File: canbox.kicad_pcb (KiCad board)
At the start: 2 copper layers, 99 x 70 mm, 125 parts, among them J1 SWD, J11 USB_B_Micro, J2 RELAY, J3 100BaseT1, J4 USB_B_Micro, J5 DB9_Male, J6 Conn_01x08_Female, J7 USB_B_Micro, J9 USB_B_Micro, K2 FTR-K3AB005W, U1 LPC54616J512, U11 MP1582EN-LF-Z, U2 DP83TC811R-Q1, U3 74LVC1G04, U5 TJA1051T/3/1J, U6 TLV70233_SOT23-5, U7 KeyMatrix, U8 ULN2003ADRG3, Y1 12MHZ, Y2 25 MHz

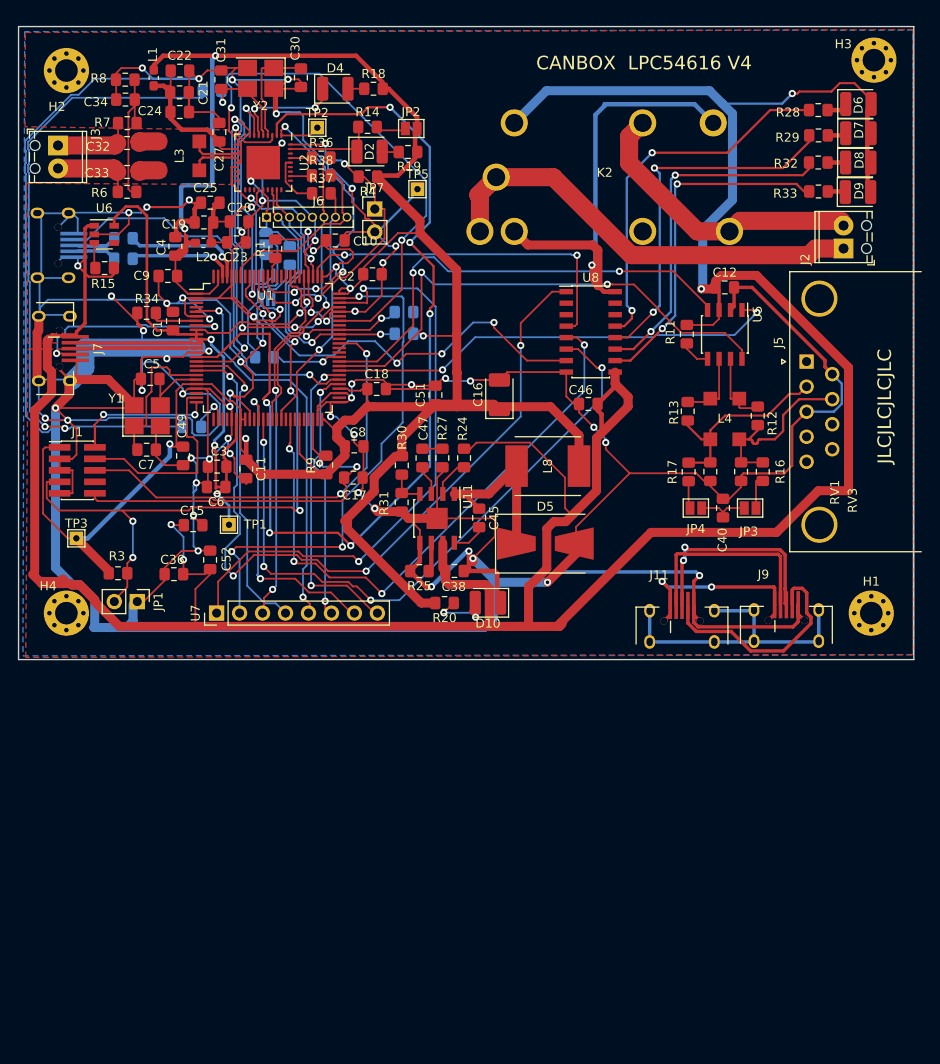
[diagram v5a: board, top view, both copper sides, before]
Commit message: Switch to 4 Layer PCB as the RMII loopback doesn't work
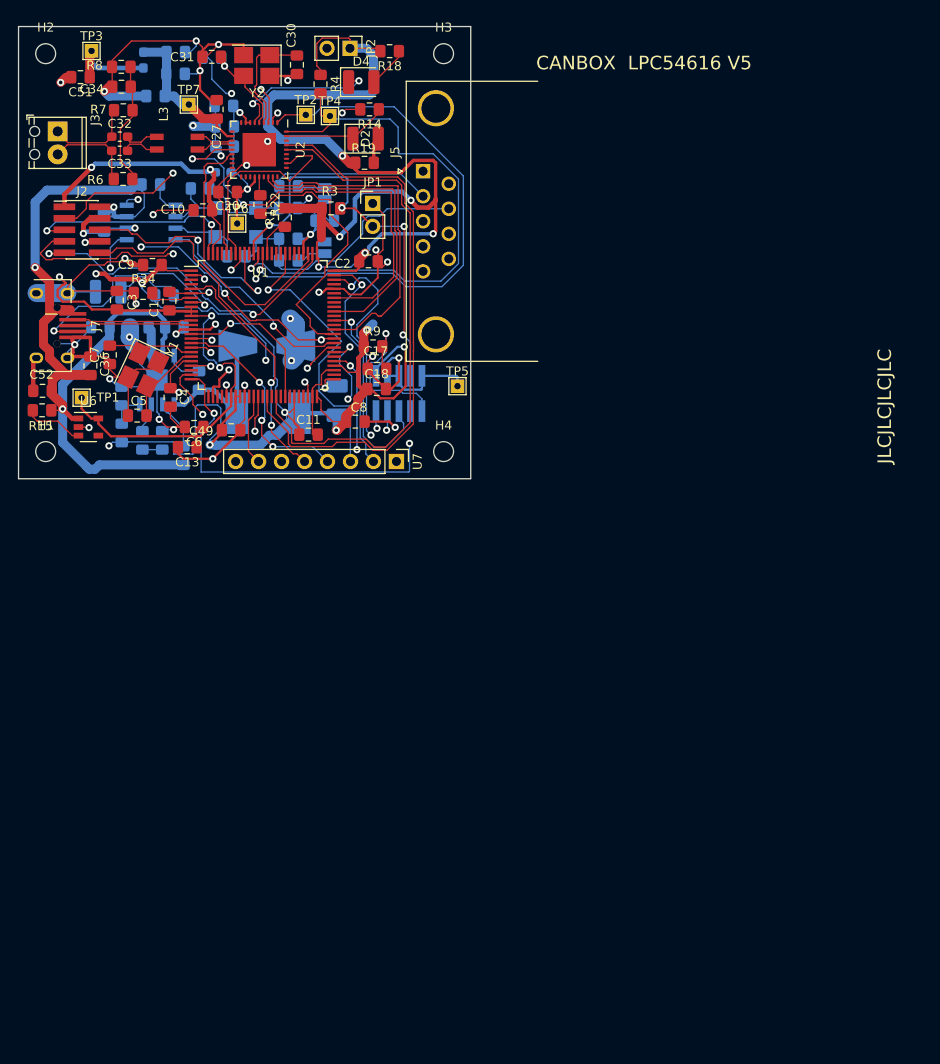
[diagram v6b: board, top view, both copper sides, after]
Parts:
- removed C15: 100n, Capacitor_SMD:C_0805_2012Metric_Pad1.15x1.40mm_HandSolder
- removed D6, D7, D8, D9: LED, LED_SMD:LED_1210_3225Metric
- removed J11, J4, J9: USB_B_Micro, cypress:MicroUsb
- removed J6: Conn_01x08_Female, Connector_PinHeader_1.27mm:PinHeader_1x08_P1.27mm_Vertical_RMII
- removed JP5: Jumper_3_Bridged12, Jumper:SolderJumper-3_P1.3mm_Open_RoundedPad1.0x1.5mm
- removed JP7: MDIO, Connector_PinHeader_2.54mm:PinHeader_1x02_P2.54mm_Vertical
- removed K2: FTR-K3AB005W, cypress:ALF1T05
- removed R10, R5: 2.49k, Resistor_SMD:R_0805_2012Metric_Pad1.15x1.40mm_HandSolder
- removed R2, R21, R23: 33, Resistor_SMD:R_0805_2012Metric_Pad1.15x1.40mm_HandSolder
- removed R28, R29, R32, R33: 300, Resistor_SMD:R_0805_2012Metric_Pad1.15x1.40mm_HandSolder
- removed R35, R36, R37, R38: NM, Resistor_SMD:R_0805_2012Metric_Pad1.15x1.40mm_HandSolder
- removed U3: 74LVC1G04, Package_TO_SOT_SMD:SOT-353_SC-70-5_Handsoldering
- removed U8: ULN2003ADRG3, Package_SO:SOIC-16_3.9x9.9mm_P1.27mm
- added C13: 4.7u, Capacitor_SMD:C_0805_2012Metric_Pad1.15x1.40mm_HandSolder, F.Cu at (38.7, 66.5)
- added TP4: MDIO, TestPoint:TestPoint_THTPad_1.5x1.5mm_Drill0.7mm, F.Cu at (54.4, 29.9)
- added TP6: ETH_IO, TestPoint:TestPoint_THTPad_1.5x1.5mm_Drill0.7mm, F.Cu at (44.2, 41.8)
- added TP7: ETH_A, TestPoint:TestPoint_THTPad_1.5x1.5mm_Drill0.7mm, F.Cu at (38.8, 28.6)
- C12, C16, C19, C21, C22, C23, C24, C25, C38, C40, C45, C46, C47, D10, D5, J1, JP3, JP4, L1, L2, L4, L8, R11, R12, R13, R16, R17, R20, R24, R25, R27, RV1, RV3, U11, U5: moved to B.Cu
- C32, C33: footprint Capacitor_SMD:C_0805_2012Metric_Pad1.15x1.40mm_HandSolder -> Capacitor_SMD:C_0603_1608Metric_Pad1.05x0.95mm_HandSolder
- C6: value 4.7u -> 10n
- H1, H2, H3, H4: value H -> MountingHole-Mechanical; footprint MountingHole:MountingHole_2.5mm_Pad_Via -> MountingHole:MountingHole_2.2mm_M2_DIN965
- J2: value RELAY -> Conn_02x05_Odd_Even; footprint TerminalBlock_Phoenix:TerminalBlock_Phoenix_MPT-0,5-2-2.54_1x02_P2.54mm_Horizontal -> Connector_PinHeader_1.27mm:PinHeader_2x05_P1.27mm_Vertical_SMD
- JP2: footprint Jumper:SolderJumper-2_P1.3mm_Open_Pad1.0x1.5mm -> Connector_PinHeader_2.54mm:PinHeader_1x02_P2.54mm_Vertical
- R22: moved to F.Cu
- R30: value 124k -> 12.4k; moved to B.Cu
- R31: value 39.2k -> 3.9k; moved to B.Cu
- moved H1 93.0 mm to (23.0, 67.0)
- moved J2 84.2 mm to (27.0, 42.5), turned to 0 degrees
- moved C12 69.0 mm to (29.5, 41.7), turned to 270 degrees
- moved U5 64.6 mm to (34.7, 41.7), turned to 0 degrees
- moved R11 61.5 mm to (34.6, 37.5), turned to 0 degrees
- moved R12 60.3 mm to (44.1, 45.4), turned to 0 degrees
- moved R13 59.3 mm to (40.1, 37.9), turned to 0 degrees
- moved L4 58.3 mm to (44.0, 41.7), turned to 180 degrees
- moved R16 57.4 mm to (49.8, 45.9), turned to 0 degrees
- moved RV3 56.3 mm to (49.8, 43.5), turned to 0 degrees
- moved JP3 55.1 mm to (53.9, 44.5), turned to 270 degrees
- moved RV1 55.0 mm to (49.8, 40.1), turned to 0 degrees
- moved C46 54.6 mm to (29.0, 53.2)
- moved R17 54.4 mm to (49.9, 37.7), turned to 0 degrees
- moved C40 54.3 mm to (53.9, 41.5), turned to 180 degrees
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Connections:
- J1 pad 8: Net-(J1-Pad8) -> (no net)
- J2 pad 1: Net-(J2-Pad1) -> +3V3
- J2 pad 2: Net-(J2-Pad2) -> +5V
- J5 pad 1: Net-(J5-Pad1) -> (no net)
- J5 pad 4: Net-(J5-Pad4) -> (no net)
- J5 pad 5: Net-(J5-Pad5) -> (no net)
- J5 pad 8: Net-(J5-Pad8) -> (no net)
- J5 pad 9: Net-(J5-Pad9) -> (no net)
- R22 pad 1: Net-(JP5-Pad2) -> /Ethernet/RGMII_CLK
- U1 pad 100: Net-(U1-Pad100) -> Net-(J2-Pad5)
- U1 pad 18: Net-(U1-Pad18) -> Net-(J2-Pad3)
- U1 pad 27: Net-(R35-Pad2) -> Net-(R26-Pad2)
- U1 pad 28: Net-(U1-Pad28) -> (no net)
- U1 pad 29: Net-(U1-Pad29) -> (no net)
- U1 pad 3: Net-(U1-Pad3) -> (no net)
- U1 pad 37: Net-(U1-Pad37) -> Net-(J2-Pad8)
- U1 pad 4: Net-(U1-Pad4) -> (no net)
- U1 pad 43: Net-(U1-Pad43) -> Net-(J2-Pad10)
- U1 pad 44: Net-(U1-Pad44) -> (no net)
- U1 pad 47: Net-(U1-Pad47) -> (no net)
- U1 pad 52: Net-(U1-Pad52) -> (no net)
- U1 pad 56: Net-(J4-Pad4) -> (no net)
- U1 pad 62: (no net) -> /Ethernet/RGMII_DO
- U1 pad 65: Net-(U1-Pad65) -> (no net)
- U1 pad 67: /Ethernet/RGMII_DO -> (no net)
- U1 pad 70: Net-(U1-Pad70) -> (no net)
- U1 pad 72: Net-(U1-Pad72) -> (no net)
- U1 pad 77: Net-(U1-Pad77) -> Net-(J2-Pad9)
- U1 pad 80: /3V3_LC -> (no net)
- U1 pad 82: Net-(U1-Pad82) -> (no net)
- U1 pad 85: Net-(U1-Pad85) -> (no net)
- U1 pad 91: Net-(U1-Pad91) -> (no net)
- U1 pad 92: Net-(U1-Pad92) -> Net-(J2-Pad6)
- U1 pad 93: Net-(U1-Pad93) -> Net-(J2-Pad7)
- U1 pad 95: Net-(U1-Pad95) -> (no net)
- U1 pad 97: /PowerSupply/USB0_D+ -> (no net)
- U1 pad 98: /PowerSupply/USB0_D- -> (no net)
- U2 pad 29: Net-(R38-Pad1) -> /Ethernet/RGMII_TX_EN
- U2 pad 32: Net-(R37-Pad1) -> /Ethernet/RGMII_TX_D1
- U2 pad 33: Net-(R36-Pad1) -> /Ethernet/RGMII_TX_D0
- U2 pad 7: Net-(U1-Pad91) -> /Ethernet/ETH_3V3
- U2 pad 8: Net-(U1-Pad72) -> /Ethernet/ETH_3V3
- U6 pad 4: Net-(U6-Pad4) -> (no net)
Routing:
- net GND: track 891.5 -> 543.5 mm, vias 60 -> 41
- net +5V: track 383.8 -> 104.9 mm, vias 5 -> 3
- net +3V3: track 317.6 -> 411.3 mm, vias 9 -> 17
- net Net-(U1-Pad18): track 84.7 -> 0.00 mm, vias 4 -> 0
- net Net-(U1-Pad37): track 72.6 -> 0.00 mm, vias 4 -> 0
- net Net-(U1-Pad15): track 112.1 -> 42.7 mm, vias 6 -> 3
- net Net-(U1-Pad43): track 66.3 -> 0.00 mm, vias 4 -> 0
- net Net-(K2-Pad1): track 50.0 -> 0.00 mm, vias 1 -> 0
- net Net-(J2-Pad1): track 49.2 -> 0.00 mm
- net Net-(U1-Pad92): track 46.5 -> 0.00 mm, vias 4 -> 0
- net Net-(J4-Pad4): track 43.1 -> 0.00 mm, vias 1 -> 0
- net Net-(R28-Pad1): track 41.2 -> 0.00 mm, vias 2 -> 0
- net Net-(R29-Pad1): track 40.9 -> 0.00 mm, vias 2 -> 0
- net Net-(J2-Pad8): track 0.00 -> 40.8 mm, vias 0 -> 2
- net Net-(J2-Pad3): track 0.00 -> 40.0 mm, vias 0 -> 2
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- added copper zone on In1.Cu, net (none)
- added copper zone on In2.Cu, net GND
- removed copper zone on B.Cu, net GND
- removed copper zone on F.Cu, net GND
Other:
- board size 99 x 70 mm -> 50 x 50 mm
- copper layers 2 -> 4
- net class Default: clearance 0.127 -> 0.2; trace_width 0.24 -> 0.146812
- net class DiffPair added: clearance 0.127, trace_width 1, via_dia 0.8, via_drill 0.4
- net class DiffPairUSB added: clearance 0.127, trace_width 1, via_dia 0.8, via_drill 0.4
- rule trace_clearance: 0.127 -> 0.2
- rule trace_min: 0.1905 -> 0.1016
- rule via_min_drill: 0.3 -> 0.4
- board text added: "CANBOX LPC54616 V5"
- board text added: "JLC2313 50 Ohm 5.78 mil 100 Ohmm 4 mil 5 mil gap"
- board text removed: "CANBOX LPC54616 V4"

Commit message: V5 now impedance controlled
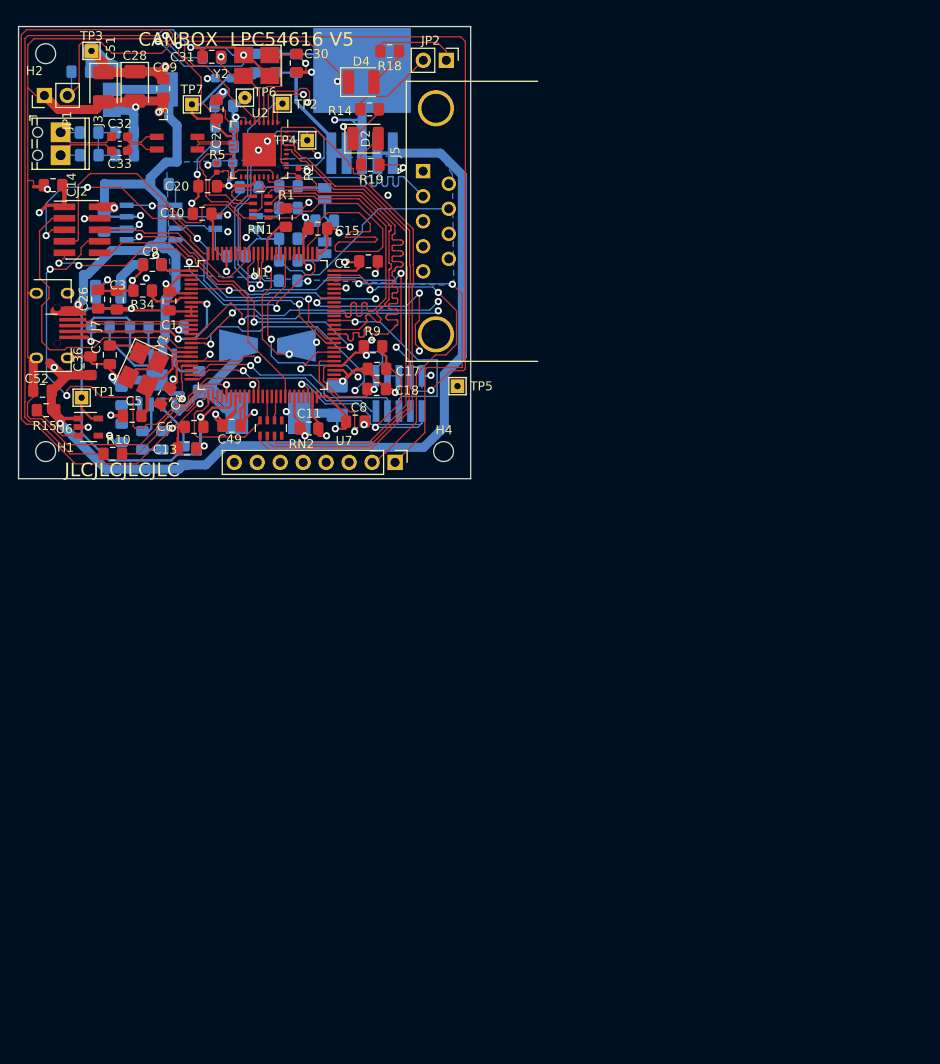
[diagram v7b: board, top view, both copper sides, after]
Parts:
- removed H3: MountingHole-Mechanical, MountingHole:MountingHole_2.2mm_M2_DIN965
- removed R22: 33, Resistor_SMD:R_0805_2012Metric_Pad1.15x1.40mm_HandSolder
- added C14: 100n, Capacitor_SMD:C_0805_2012Metric_Pad1.15x1.40mm_HandSolder, F.Cu at (23.8, 37.5)
- added C15: 100n, Capacitor_SMD:C_0805_2012Metric_Pad1.15x1.40mm_HandSolder, F.Cu at (53.1, 42.3)
- added C26: 100n, Capacitor_SMD:C_0805_2012Metric_Pad1.15x1.40mm_HandSolder, F.Cu at (28.8, 50.2)
- added C28: NM, Capacitor_Tantalum_SMD:CP_EIA-3528-21_Kemet-B_Pad1.50x2.35mm_HandSolder, F.Cu at (32.9, 26.6)
- added C29: NM, Capacitor_SMD:C_0805_2012Metric_Pad1.15x1.40mm_HandSolder, F.Cu at (36.0, 26.9)
- added R10: NM, Resistor_SMD:R_0805_2012Metric_Pad1.15x1.40mm_HandSolder, F.Cu at (30.4, 67.2)
- added R2: 2.49k, Resistor_SMD:R_0402_1005Metric, F.Cu at (50.9, 36.2)
- added R5: 2.49k, Resistor_SMD:R_0402_1005Metric, F.Cu at (41.9, 35.6)
- added RN1: 50, Resistor_SMD:R_Array_Concave_4x0603, F.Cu at (46.8, 40.0)
- added RN2: 50, Resistor_SMD:R_Array_Concave_4x0603, F.Cu at (47.9, 64.4)
- added U3: TL1963A, Package_TO_SOT_SMD:TO-263-5_TabPin3, B.Cu at (58.0, 28.2)
- added U4: AP2114H-3.3, Package_TO_SOT_SMD:SOT-223-3_TabPin2, B.Cu at (33.5, 27.0)
- C34, R3, R4, R6, R7, R8: moved to B.Cu
- C51: footprint Capacitor_SMD:C_0805_2012Metric_Pad1.15x1.40mm_HandSolder -> Capacitor_Tantalum_SMD:CP_EIA-3528-21_Kemet-B_Pad1.50x2.35mm_HandSolder
- L3, L4: footprint Inductor_SMD:L_CMC_1812 -> cypress:L_CMC_1812
- moved JP1 38.2 mm to (22.9, 27.6), turned to 90 degrees
- moved R3 31.5 mm to (26.9, 25.0), turned to 0 degrees
- moved R4 22.0 mm to (49.8, 48.1), turned to 180 degrees
- moved C24 16.0 mm to (50.7, 24.1), turned to 90 degrees
- moved TP6 13.9 mm to (45.0, 27.9)
- moved C22 11.1 mm to (48.5, 24.0), turned to 90 degrees
- moved JP2 10.7 mm to (67.3, 23.7)
- moved R8 9.79 mm to (31.7, 34.2), turned to 0 degrees
- moved L1 9.05 mm to (42.6, 25.7), turned to 0 degrees
- moved C21 8.90 mm to (46.2, 24.0), turned to 90 degrees
- moved R13 5.43 mm to (45.5, 37.8)
- moved C34 5.08 mm to (31.7, 31.7), turned to 180 degrees
- moved R6 4.56 mm to (27.8, 34.2)
- moved R7 4.52 mm to (27.8, 31.7)
- moved TP4 3.68 mm to (51.9, 32.6)
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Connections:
- R26 pad 2: Net-(R26-Pad2) -> Net-(R10-Pad1)
- U1 pad 26: (no net) -> Net-(RN2-Pad4)
- U1 pad 27: Net-(R26-Pad2) -> Net-(R10-Pad2)
- U1 pad 39: /Ethernet/RGMII_TX_D0 -> Net-(RN2-Pad3)
- U1 pad 41: /Ethernet/RGMII_TX_D1 -> Net-(RN2-Pad2)
- U1 pad 62: /Ethernet/RGMII_DO -> Net-(RN1-Pad7)
- U1 pad 66: /Ethernet/RGMII_D1 -> Net-(RN1-Pad6)
- U1 pad 78: /Ethernet/RGMII_DV -> Net-(RN1-Pad5)
- U1 pad 94: /Ethernet/RGMII_TX_EN -> (no net)
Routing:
- net GND: track 543.5 -> 796.2 mm, vias 41 -> 47
- net +3V3: track 411.3 -> 558.4 mm, vias 17 -> 23
- net +5V: track 104.9 -> 194.2 mm, vias 3 -> 5
- net Net-(J1-Pad7): track 45.6 -> 132.4 mm
- net Net-(R10-Pad1): track 0.00 -> 73.4 mm, vias 0 -> 1
- net Net-(U1-Pad69): track 47.9 -> 108.1 mm, vias 2 -> 4
- net Net-(RN1-Pad5): track 0.00 -> 45.6 mm
- net Net-(U1-Pad15): track 42.7 -> 88.0 mm
- net Net-(R26-Pad2): track 43.1 -> 0.00 mm, vias 2 -> 0
- net Net-(U1-Pad16): track 45.7 -> 87.1 mm, vias 2 -> 3
- net /Ethernet/RGMII_TX_EN: track 23.2 -> 63.6 mm
- net Net-(RN1-Pad6): track 0.00 -> 34.8 mm
- net /Ethernet/MDIO: track 64.6 -> 30.0 mm
- net Net-(RN1-Pad7): track 0.00 -> 34.0 mm
- net /Ethernet/MDC: track 60.8 -> 30.6 mm
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- added copper zone on In2.Cu, net +3V3
- added copper zone on B.Cu, net GND
- added copper zone on In1.Cu, net GND
- removed copper zone on In1.Cu, net (none)
- removed copper zone on In2.Cu, net GND
